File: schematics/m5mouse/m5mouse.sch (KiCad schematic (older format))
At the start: 53 parts, among them IC1 LM3940IMP-3.3_NOPB, J1 Conn_01x02, J2 M-BUS, J3 SWD, J6 Conn_01x03, J7 Conn_01x06, J8 Conn_01x06, SW1 SW_SPDT, SW2 SW_Push, U1 TPS562200, U2 STM32F405RGTx, Y1 8MHz, Y2 32.768kHz

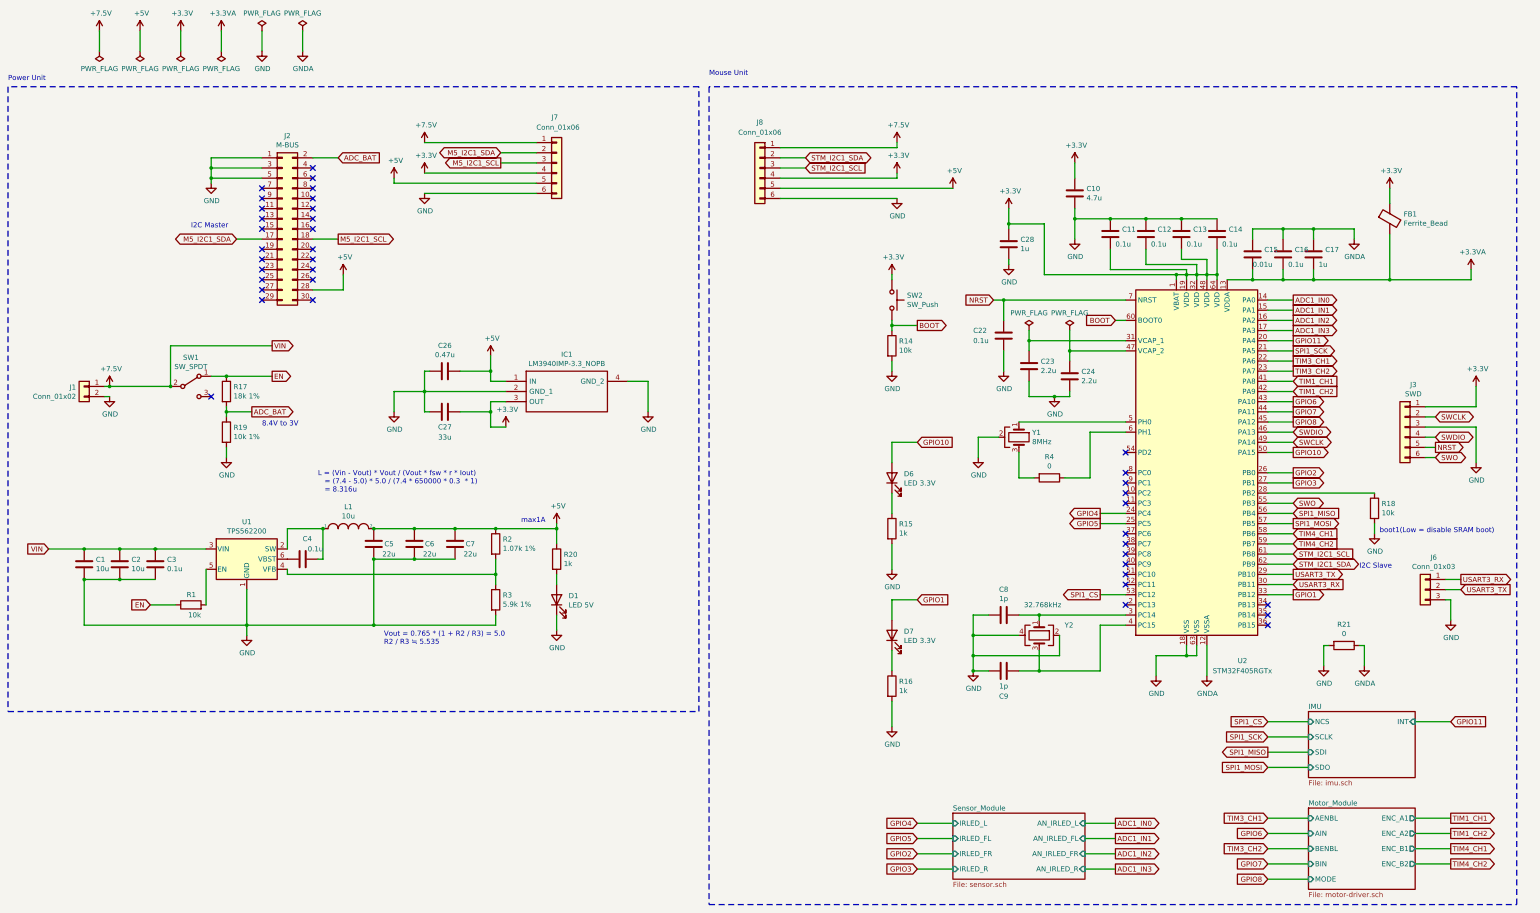
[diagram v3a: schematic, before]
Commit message: Fix flipped pin header
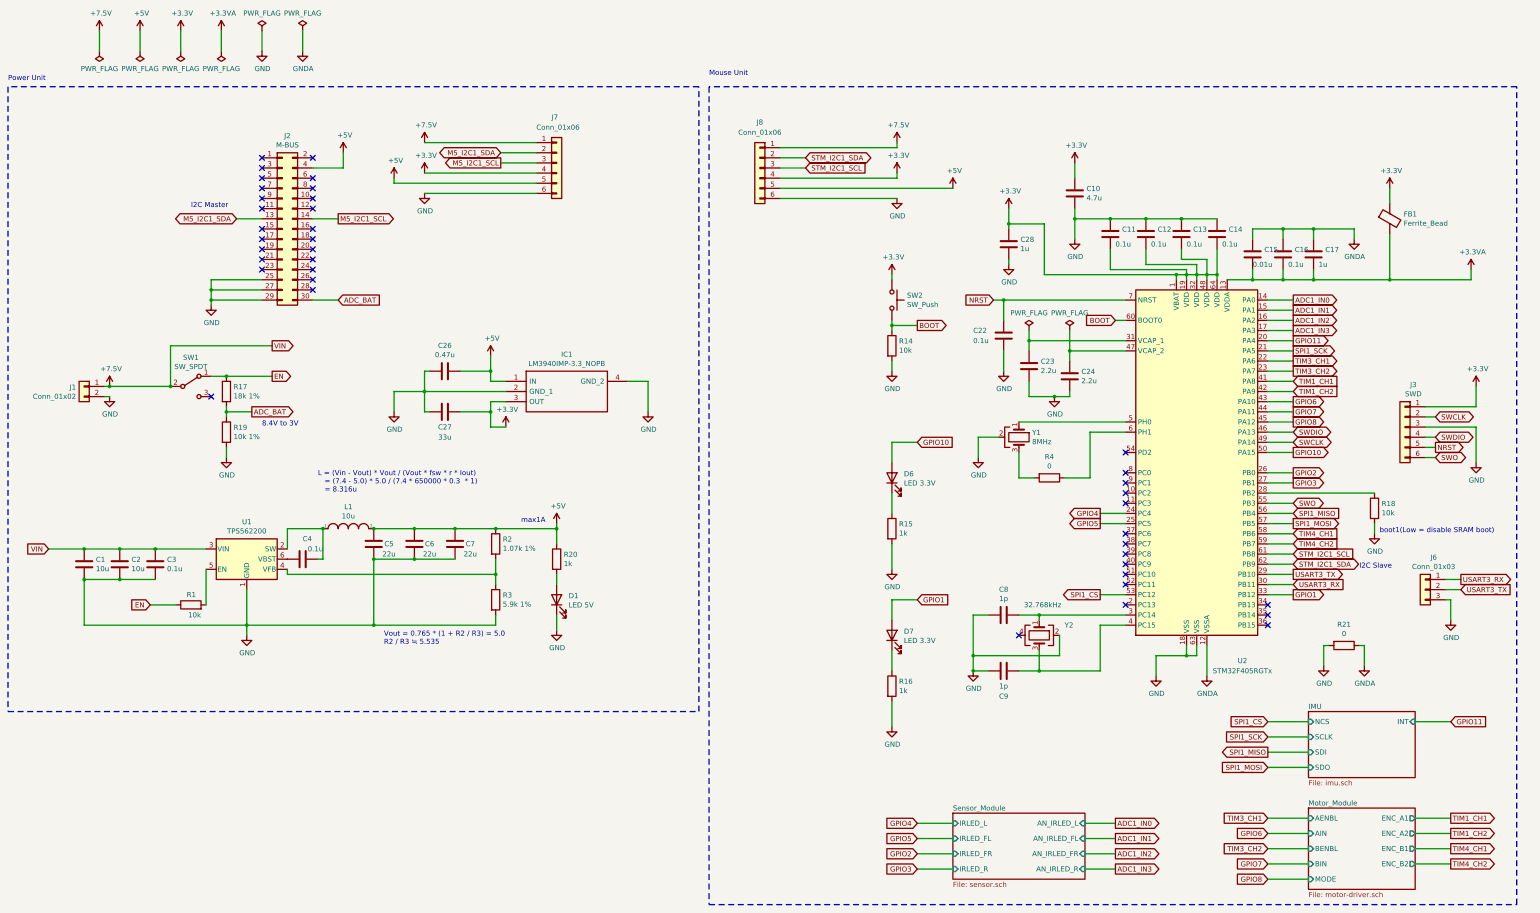
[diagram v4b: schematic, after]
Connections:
- net +5V: now also J2.4 (Pin_4); no longer J2.28 (Pin_28)
- net ADC_BAT: now also J2.30 (Pin_30); no longer J2.2 (Pin_2)
- net GND: now also J2.25 (Pin_25), J2.27 (Pin_27), J2.29 (Pin_29); no longer J2.1 (Pin_1), J2.3 (Pin_3), J2.5 (Pin_5), Y2.4
- net M5_I2C1_SCL: now also J2.14 (Pin_14); no longer J2.18 (Pin_18)
- net M5_I2C1_SDA: now also J2.13 (Pin_13); no longer J2.17 (Pin_17)
- no-connect marks 39 -> 40
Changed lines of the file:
@@
 EndData
 $EndBitmap
-Text GLabel 2850 3200 0    50   BiDi ~ 0
+Text GLabel 2850 3000 0    50   BiDi ~ 0
 M5_I2C1_SDA
 Wire Wire Line
-	2850 3200 3100 3200
-Text GLabel 3850 3200 2    50   Output ~ 0
+	2850 3000 3100 3000
+Text GLabel 3850 3000 2    50   Output ~ 0
 M5_I2C1_SCL
 Wire Wire Line
-	3600 3200 3850 3200
+	3600 3000 3850 3000
 $Comp
 L Connector_Generic:Conn_02x15_Odd_Even J2
@@
 Text Notes 13900 6450 0    50   ~ 0
 I2C Slave
-Text Notes 2400 3100 0    50   ~ 0
+Text Notes 2400 2900 0    50   ~ 0
 I2C Master
 NoConn ~ 13000 6900
@@
 NoConn ~ 3600 3300
 NoConn ~ 3600 3100
-NoConn ~ 3600 3000
 NoConn ~ 3600 2900
 NoConn ~ 3600 2800
 NoConn ~ 3600 2700
 NoConn ~ 3600 2600
-NoConn ~ 3600 2500
-$Comp
-L power:GND #PWR0118
-U 1 1 5F16FAC2
-P 2600 2650
-F 0 "#PWR0118" H 2600 2400 50  0001 C CNN
-F 1 "GND" H 2605 2477 50  0000 C CNN
-F 2 "" H 2600 2650 50  0001 C CNN
-F 3 "" H 2600 2650 50  0001 C CNN
-	1    2600 2650
-	1    0    0    -1
-$EndComp
 NoConn ~ 3100 2700
 NoConn ~ 3100 2800
 NoConn ~ 3100 2900
-NoConn ~ 3100 3000
 NoConn ~ 3100 3100
 NoConn ~ 3100 3300
 NoConn ~ 3100 3400
 NoConn ~ 3100 3500
-NoConn ~ 3100 3600
-NoConn ~ 3100 3700
-NoConn ~ 3100 3800
-Wire Wire Line
-	2600 2600 2600 2650
-Wire Wire Line
-	2600 2600 3100 2600
-Wire Wire Line
-	2600 2500 2600 2600
-Wire Wire Line
-	2600 2500 3100 2500
-Connection ~ 2600 2600
-Wire Wire Line
-	3100 2400 2600 2400
-Wire Wire Line
-	2600 2400 2600 2500
-Connection ~ 2600 2500
 $Comp
 L Connector_Generic:Conn_01x03 J6
@@
 L power:+5V #PWR011
 U 1 1 5F219F14
-P 3900 3550
-F 0 "#PWR011" H 3900 3400 50  0001 C CNN
-F 1 "+5V" H 3915 3723 50  0000 C CNN
-F 2 "" H 3900 3550 50  0001 C CNN
-F 3 "" H 3900 3550 50  0001 C CNN
-	1    3900 3550
+P 3900 2350
+F 0 "#PWR011" H 3900 2200 50  0001 C CNN
+F 1 "+5V" H 3915 2523 50  0000 C CNN
+F 2 "" H 3900 2350 50  0001 C CNN
+F 3 "" H 3900 2350 50  0001 C CNN
+	1    3900 2350
 	1    0    0    -1
 $EndComp
 Wire Wire Line
-	3900 3550 3900 3700
+	3900 2350 3900 2500
 Wire Wire Line
-	3900 3700 3600 3700
+	3900 2500 3600 2500
 $Comp
 L power:+5V #PWR012
@@
 	1    0    0    -1
 $EndComp
-NoConn ~ 3600 3800
 Wire Wire Line
 	13000 4600 13250 4600
@@
 EndData
 $EndBitmap
-Text GLabel 3850 2400 2    50   Input ~ 0
+Text GLabel 3850 3800 2    50   Input ~ 0
 ADC_BAT
 Wire Wire Line
-	3850 2400 3600 2400
+	3850 3800 3600 3800
 $Comp
 L Device:R R19
@@
 	10950 7300 10100 7300
 Connection ~ 10100 7300
-Wire Wire Line
-	10100 7300 10100 7100
-Wire Wire Line
-	10550 7100 10100 7100
-Connection ~ 10100 7100
-Wire Wire Line
-	10100 7100 10100 6900
 NoConn ~ 11600 6800
 Wire Wire Line
@@
 	0    1    1    0
 $EndComp
+Connection ~ 2600 3700
+Wire Wire Line
+	2600 3600 2600 3700
+Wire Wire Line
+	3100 3600 2600 3600
+Connection ~ 2600 3800
+Wire Wire Line
+	2600 3700 3100 3700
+Wire Wire Line
+	2600 3700 2600 3800
+Wire Wire Line
+	2600 3800 3100 3800
+Wire Wire Line
+	2600 3800 2600 3850
+$Comp
+L power:GND #PWR0118
+U 1 1 5F16FAC2
+P 2600 3850
+F 0 "#PWR0118" H 2600 3600 50  0001 C CNN
+F 1 "GND" H 2605 3677 50  0000 C CNN
+F 2 "" H 2600 3850 50  0001 C CNN
+F 3 "" H 2600 3850 50  0001 C CNN
+	1    2600 3850
+	1    0    0    -1
+$EndComp
+NoConn ~ 3600 2400
+NoConn ~ 3100 2400
+NoConn ~ 3100 2500
+NoConn ~ 3100 2600
+NoConn ~ 3600 3700
+NoConn ~ 3100 3200
+NoConn ~ 3600 3200
+Wire Wire Line
+	10100 6900 10100 7300
+NoConn ~ 10550 7100
 $EndSCHEMATC

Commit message: Fix schematics
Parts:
- added J10, J11: Conn_01x03, Connector_PinSocket_2.54mm:PinSocket_1x03_P2.54mm_Vertical, symbol Connector_Generic:Conn_01x03
- added J9: Conn_01x03, Connector_PinHeader_2.54mm:PinHeader_1x03_P2.54mm_Vertical, symbol Connector_Generic:Conn_01x03
- J1: footprint Connector_JST:JST_PH_B2B-PH-K_1x02_P2.00mm_Vertical -> Connector_JST:JST_PH_S2B-PH-K_1x02_P2.00mm_Horizontal
- J3: Manf# B6B-EH-A -> S6B-EH(LF)(SN); URL https://www.digikey.jp/product-detail/ja/jst-sales-america-inc/B6B-EH-A/455-1018-ND/527242 -> https://www.digikey.jp/product-detail/ja/jst-sales-america-inc/S6B-EH-LF-SN/455-1629-ND/926537
- J6: Manf# 61300311121 -> (none); URL https://www.digikey.jp/product-detail/ja/w%C3%BCrth-elektro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 -> (none)
- R2: value 1.07k 1% -> 5.9k 1%; Manf# RC0603FR-071K07L -> RC0603FR-075K9L; URL https://www.digikey.jp/product-detail/ja/yageo/RC0603FR-071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 -> https://www.digikey.jp/product-detail/ja/yageo/RC0603FR-075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
- R3: value 5.9k 1% -> 1.07k 1%; Manf# RC0603FR-075K9L -> RC0603FR-071K07L; URL https://www.digikey.jp/product-detail/ja/yageo/RC0603FR-075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 -> https://www.digikey.jp/product-detail/ja/yageo/RC0603FR-071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
- SW1: footprint Button_Switch_THT:SW_E-Switch_EG1224_SPDT_Angled -> Button_Switch_THT:SW_CuK_OS102011MA1QN1_SPDT_Angled
- SW2: footprint Button_Switch_THT:SW_PUSH_6mm -> Button_Switch_THT:SW_Tactile_SPST_Angled_PTS645Vx39-2LFS
- U1: symbol Regulator_Switching:TPS562200 -> m5mouse-rescue:TPS562200-Regulator_Switching
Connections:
- net +5V: now also J11.1 (Pin_1), J9.1 (Pin_1); no longer J7.5 (Pin_5), J8.5 (Pin_5)
- net +7.5V: now also J6.1 (Pin_1), J10.1 (Pin_1); no longer J7.1 (Pin_1), J8.1 (Pin_1)
- net GND: now also J10.3 (Pin_3), J11.3 (Pin_3), J9.3 (Pin_3)
- net USART3_RX: no longer names the net of U2.30 (PB11)
- net USART3_RX: no longer J6.1 (Pin_1)
- net USART3_TX: no longer names the net of U2.29 (PB10)
- net USART3_TX: no longer J6.2 (Pin_2)
- no-connect marks 40 -> 50
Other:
- moved on the sheet: C26, C27, IC1, J7

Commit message: Fix path
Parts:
- SW1: Manf# EG1224 -> OS102011MA1QN1; URL https://www.digikey.jp/product-detail/ja/e-switch/EG1224/EG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 -> https://www.digikey.jp/products/ja?keywords=OS102011MA1QN1
- SW2: Manf# 1825910-7 -> PTS645VL39-2 LFS; URL https://www.digikey.jp/product-detail/ja/te-connectivity-al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 -> https://www.digikey.jp/product-detail/ja/c-k/PTS645VL39-2-L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
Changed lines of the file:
@@
 F 2 "Button_Switch_THT:SW_Tactile_SPST_Angled_PTS645Vx39-2LFS" H 9300 4000 50  0001 C CNN
 F 3 "~" H 9300 4000 50  0001 C CNN
-F 4 "1825910-7" V 9300 3800 50  0001 C CNN "Manf#"
-F 5 "https://www.digikey.jp/product-detail/ja/te-connectivity-alcoswitch-switches/1825910-7/450-1804-ND/1731414" V 9300 3800 50  0001 C CNN "URL"
+F 4 "PTS645VL39-2 LFS" V 9300 3800 50  0001 C CNN "Manf#"
+F 5 "https://www.digikey.jp/product-detail/ja/c-k/PTS645VL39-2-LFS/CKN9103-ND/1146765" V 9300 3800 50  0001 C CNN "URL"
 	1    9300 3800
 	0    1    1    0
@@
 F 2 "Button_Switch_THT:SW_CuK_OS102011MA1QN1_SPDT_Angled" H 2400 4650 50  0001 C CNN
 F 3 "~" H 2400 4650 50  0001 C CNN
-F 4 "EG1224" H 2400 4650 50  0001 C CNN "Manf#"
-F 5 "https://www.digikey.jp/product-detail/ja/e-switch/EG1224/EG2585-ND/502052?utm_adgroup=Switches&utm_source=google&utm_medium=cpc&utm_campaign=Dynamic%20Search_JP&utm_term=&productid=&gclid=CjwKCAjwnef6BRAgEiwAgv8mQUfr-xcs4CYH2XBHdbgL7JDyCOFgnaAjsRusl37e-Kt1f0lrQ_MqJRoCD-0QAvD_BwE" H 2400 4650 50  0001 C CNN "URL"
+F 4 "OS102011MA1QN1" H 2400 4650 50  0001 C CNN "Manf#"
+F 5 "https://www.digikey.jp/products/ja?keywords=OS102011MA1QN1" H 2400 4650 50  0001 C CNN "URL"
 	1    2400 4650
 	1    0    0    -1

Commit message: Fix connector
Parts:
- J10, J11: Manf# (none) -> PPPC031LFBN-RC; URL (none) -> https://www.digikey.jp/product-detail/ja/sullins-connector-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
- J6: Manf# (none) -> PRPC003SAAN-RC; URL (none) -> https://www.digikey.jp/product-detail/ja/sullins-connector-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
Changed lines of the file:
@@
 F 2 "Connector_PinHeader_2.54mm:PinHeader_1x03_P2.54mm_Vertical" H 8200 3650 50  0001 C CNN
 F 3 "~" H 8200 3650 50  0001 C CNN
+F 4 "PRPC003SAAN-RC" H 8200 3650 50  0001 C CNN "Manf#"
+F 5 "https://www.digikey.jp/product-detail/ja/sullins-connector-solutions/PRPC003SAAN-RC/S1011EC-03-ND/2775251" H 8200 3650 50  0001 C CNN "URL"
 	1    8200 3650
 	-1   0    0    1
@@
 F 2 "Connector_PinSocket_2.54mm:PinSocket_1x03_P2.54mm_Vertical" H 6700 3250 50  0001 C CNN
 F 3 "~" H 6700 3250 50  0001 C CNN
+F 4 "PPPC031LFBN-RC" H 6700 3250 50  0001 C CNN "Manf#"
+F 5 "https://www.digikey.jp/product-detail/ja/sullins-connector-solutions/PPPC031LFBN-RC/S7036-ND/810175" H 6700 3250 50  0001 C CNN "URL"
 	1    6700 3250
 	1    0    0    -1
@@
 F 2 "Connector_PinSocket_2.54mm:PinSocket_1x03_P2.54mm_Vertical" H 6900 4200 50  0001 C CNN
 F 3 "~" H 6900 4200 50  0001 C CNN
+F 4 "PPPC031LFBN-RC" H 6900 4200 50  0001 C CNN "Manf#"
+F 5 "https://www.digikey.jp/product-detail/ja/sullins-connector-solutions/PPPC031LFBN-RC/S7036-ND/810175" H 6900 4200 50  0001 C CNN "URL"
 	1    6900 4200
 	1    0    0    -1
